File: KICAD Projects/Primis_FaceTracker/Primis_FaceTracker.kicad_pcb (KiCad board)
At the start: 2 copper layers, 95 x 56 mm, 48 parts, among them CN2 KH-FG0.5-H2.0-24PIN, J1 USB_C_Receptacle_USB2.0_16P, Q1 PMOS, SW1 SW_SPST, SW2 SW_SPST, U1 ESP32-S3-WROOM-1, U2 AMS1117-3.3, U3 XC6206P122MR, U5 XC6206P282MR

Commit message: Face Tracker and Versipellis Clean
-Organised the face tracker PCB a bit more
-Added TODO to face tracker README
-Organised Versipellis schematics
-Updated images
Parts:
- renumbered SW2 to Boot, SW1 to Reset
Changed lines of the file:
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@@
 		(tags "resistor")
 		(property "Reference" "R13"
-			(at 0 -1.65 0)
+			(at -0.0125 1.7 0)
 			(layer "F.SilkS")
 			(effects
@@
 		(tags "usb usb-c 2.0 pd")
 		(property "Reference" "J1"
-			(at 0 -5.645 0)
+			(at -6.43 -0.95 0)
 			(layer "F.SilkS")
 			(effects
@@
 			(at 0 -3.15 0)
 			(layer "F.SilkS")
+			(hide yes)
 			(effects
 				(font
@@
 		(tags "resistor")
 		(property "Reference" "R12"
-			(at 0 -1.65 0)
+			(at -0.0125 1.7 0)
 			(layer "F.SilkS")
 			(effects
@@
 		(tags "capacitor")
 		(property "Reference" "C14"
-			(at 0 1.4 0)
+			(at 4.025 0.1 0)
 			(layer "F.SilkS")
 			(effects
@@
 		(descr "SMD Tactile Switch, 3.9x3x2 mm, https://lcsc.com/datasheet/lcsc_datasheet_2504101957_XUNPU-TS-1088-AR02016_C720477.pdf")
 		(tags "Tactile Switch")
-		(property "Reference" "SW1"
+		(property "Reference" "Reset"
 			(at 0 -2.65 0)
 			(layer "F.SilkS")
@@
 		(descr "SMD Tactile Switch, 3.9x3x2 mm, https://lcsc.com/datasheet/lcsc_datasheet_2504101957_XUNPU-TS-1088-AR02016_C720477.pdf")
 		(tags "Tactile Switch")
-		(property "Reference" "SW2"
-			(at 0 -2.65 0)
+		(property "Reference" "Boot"
+			(at 0 2.6 0)
 			(layer "F.SilkS")
 			(effects
@@
 		(tags "resistor")
 		(property "Reference" "R15"
-			(at 0 -1.65 0)
+			(at -3.2875 0 0)
 			(layer "F.SilkS")
 			(effects
@@
 			(at 0 -3.15 0)
 			(layer "F.SilkS")
+			(hide yes)
 			(effects
 				(font
@@
 		(tags "resistor")
 		(property "Reference" "R14"
-			(at 0 1.8 90)
+			(at 0.05 -1.85 90)
 			(layer "F.SilkS")
 			(effects
@@
 		(tags "capacitor")
 		(property "Reference" "C15"
-			(at 0 -1.43 0)
+			(at 3.975 0.15 0)
 			(layer "F.SilkS")
 			(effects
@@
 		(at 162.75 110.8435 180)
 		(property "Reference" "CN2"
-			(at 0 -3.65 0)
+			(at -10.25 3.3435 0)
 			(layer "F.SilkS")
 			(effects
@@
 			(at 0 -3.15 0)
 			(layer "F.SilkS")
+			(hide yes)
 			(effects
 				(font
@@
 			(at 0 -3.15 0)
 			(layer "F.SilkS")
+			(hide yes)
 			(effects
 				(font

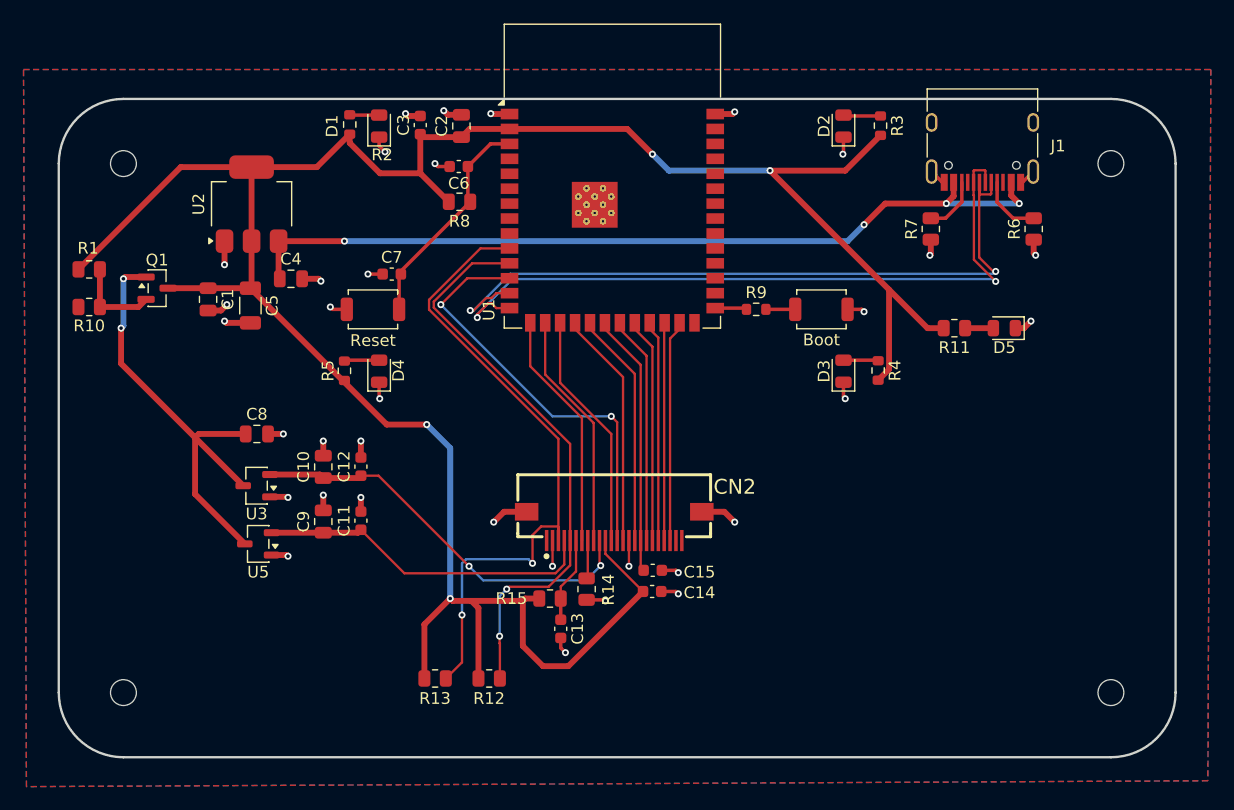
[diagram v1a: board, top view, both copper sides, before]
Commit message: Gerbers plus clean up
-Added gerbers for the face tracker and versipellis
-Shrunk the face tracker and cleaned up
-Fixed some DRC issues with both projects
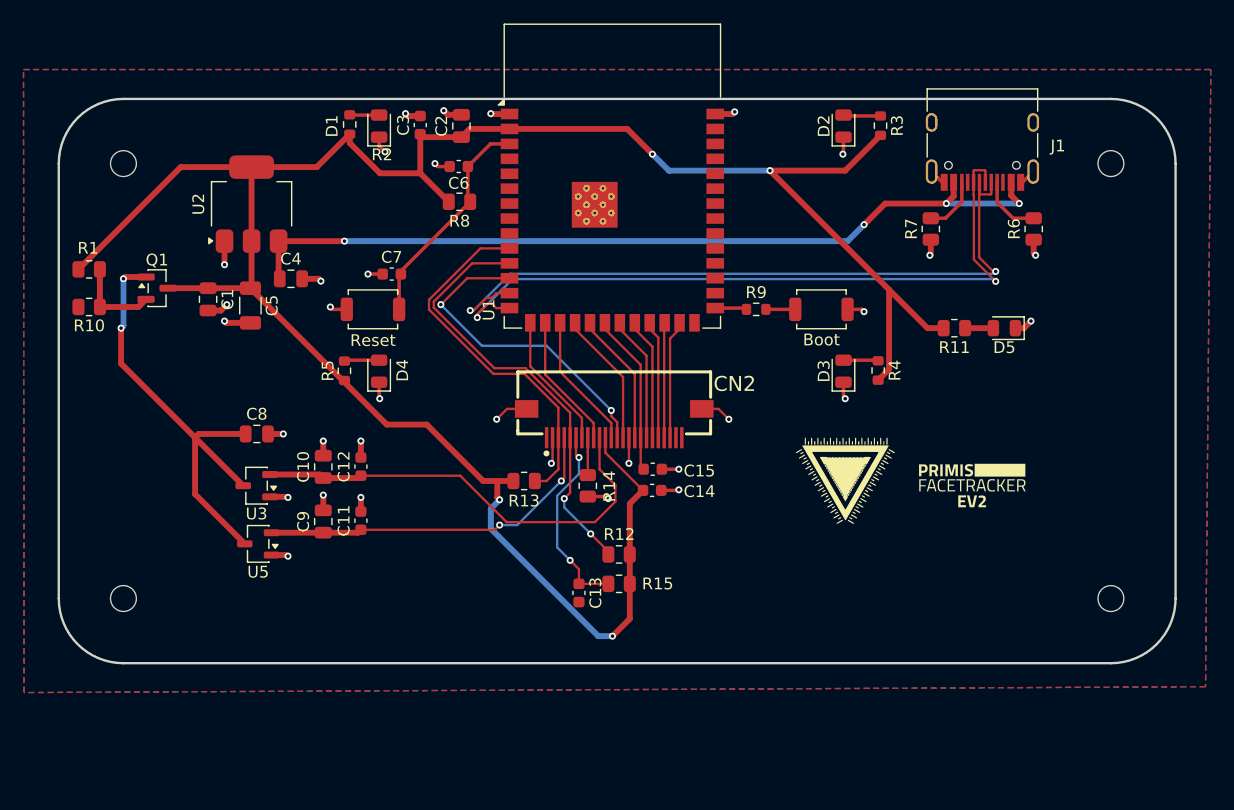
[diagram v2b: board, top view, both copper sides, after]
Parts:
- added G***: LOGO, LOGO, F.Cu at (193.2, 107.4)
- added G***: LOGO, LOGO, F.Cu at (182.4, 107.0)
- moved R13 18.4 mm to (155.1, 107.0)
- moved R12 15.3 mm to (163.2, 113.2), turned to 180 degrees
- moved R14 8.79 mm to (160.5, 107.4)
- moved CN2 8.75 mm to (162.8, 102.1)
- moved C14 8.60 mm to (166.0, 107.8)
- moved C15 8.60 mm to (166.0, 106.0)
- moved H3 8.00 mm to (121.0, 117.0)
- moved H4 8.00 mm to (205.0, 117.0)
- moved R15 6.01 mm to (163.2, 115.8), turned to 180 degrees
- moved C13 3.42 mm to (159.8, 116.5)
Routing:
- net CAM_SDA: track 56.4 -> 31.5 mm, vias 2 -> 0
- net +3V3: track 211.3 -> 197.5 mm
- net CAM_SCK: track 49.1 -> 37.4 mm
- net CAM_RST: track 7.27 -> 16.6 mm, vias 0 -> 2
- net CAM_D2: track 18.9 -> 10.1 mm
- net CAM_VSYNC: track 20.3 -> 11.6 mm
- net CAM_HSYNC: track 20.2 -> 11.5 mm
- net CAM_D6: track 20.2 -> 11.5 mm
- net CAM_D5: track 20.1 -> 11.4 mm
- net CAM_D4: track 19.5 -> 10.7 mm
- net CAM_D3: track 18.8 -> 10.1 mm
- net CAM_D1: track 18.5 -> 9.79 mm
- net CAM_D0: track 19.1 -> 10.4 mm
- net CAM_D7: track 20.3 -> 11.6 mm
- net CAM_PCLK: track 22.4 -> 13.8 mm
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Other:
- board size 95 x 56 mm -> 95 x 48 mm

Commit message: Quick Update
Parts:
- renumbered Reset to SW1, Boot to SW2
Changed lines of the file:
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@@
 		(descr "SMD Tactile Switch, 3.9x3x2 mm, https://lcsc.com/datasheet/lcsc_datasheet_2504101957_XUNPU-TS-1088-AR02016_C720477.pdf")
 		(tags "Tactile Switch")
-		(property "Reference" "Reset"
+		(property "Reference" "SW1"
 			(at 0 -2.65 0)
 			(layer "F.SilkS")
@@
 		(descr "SMD Tactile Switch, 3.9x3x2 mm, https://lcsc.com/datasheet/lcsc_datasheet_2504101957_XUNPU-TS-1088-AR02016_C720477.pdf")
 		(tags "Tactile Switch")
-		(property "Reference" "Boot"
-			(at 0 2.6 0)
-			(layer "F.SilkS")
-			(effects
+		(property "Reference" "SW2"
+			(at -0.175 -2.6 0)
+			(layer "F.SilkS")
+			(effects

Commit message: FaceTracker fixes and Dongle rework
-Fixed some mistakes on the Facetracker with the camera power lines.
-Some part swaps and additions on the dongle to match the JLCPCBs catalogue
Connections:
- U1 pad 9: unconnected-(U1-IO16-Pad9) -> CAM_PWR
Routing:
- net CAM_PWR: track 0.00 -> 43.7 mm, vias 0 -> 2
